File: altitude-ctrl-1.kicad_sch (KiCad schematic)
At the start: 92 parts, among them J1 Conn_01x02, J11 Conn_01x05, J2 TC2030, J3 Conn_01x02, J4 Conn_01x02, J5 Conn_01x04_Pin, J6 Conn_01x02, J7 Conn_01x02, J8 Conn_01x05, J9 Conn_01x05, SW1 SW_Push, SW2 SW_Push, SW3 SW_Push, SW4 SW_SPST, SW5 SW_SPST, U1 SN65HVD230, U2 LM73100, U3 HT753-1, U4 STM32F103C8Tx, U5 LM73100, U6 MAX6675, U8 ULN2003A, Y1 8M

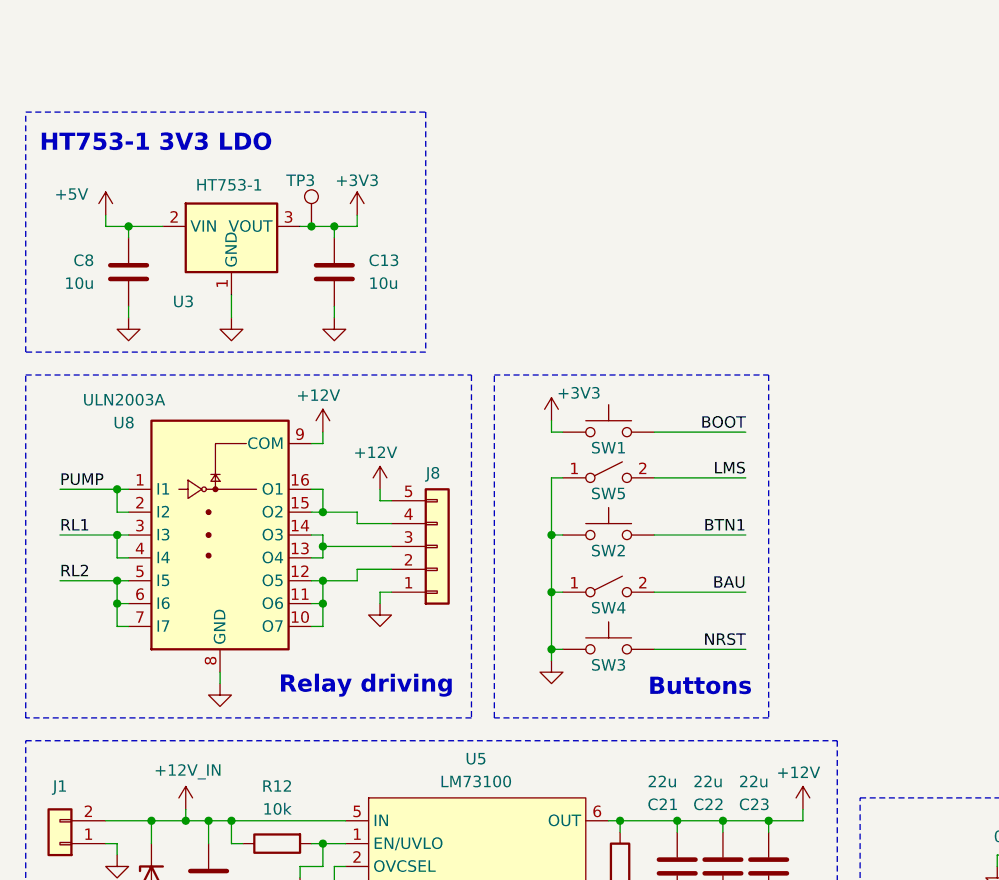
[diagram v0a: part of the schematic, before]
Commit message: schem: add test points
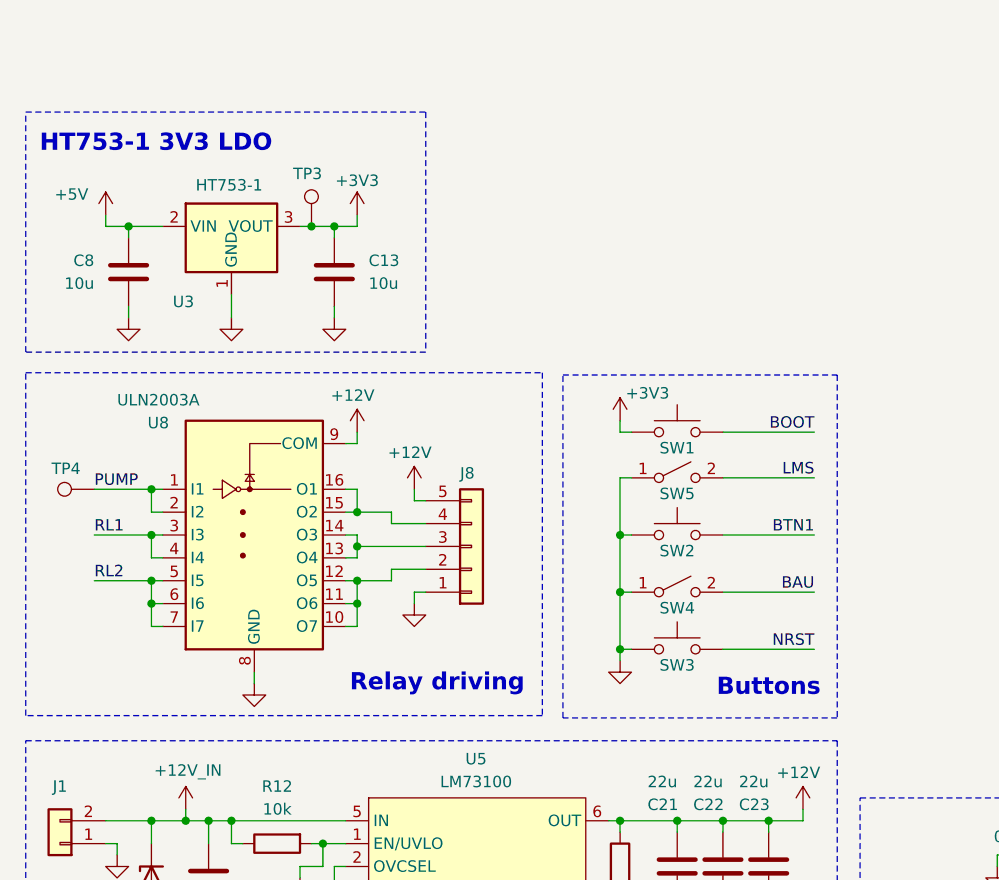
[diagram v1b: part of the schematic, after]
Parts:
- added TP4: TestPoint, TestPoint:TestPoint_Pad_D2.0mm, symbol Connector:TestPoint
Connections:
- net PUMP: now also TP4.1
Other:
- moved on the sheet: J8, SW1, SW2, SW3, SW4, SW5, U8

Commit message: schem: run and fix ERC
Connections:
- no-connect marks 14 -> 15

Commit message: schem: add missing footprints
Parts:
- J1, J6, J7, SW4, SW5, TC1: footprint (none) -> TerminalBlock_Phoenix:TerminalBlock_Phoenix_MKDS-1,5-2-5.08_1x02_P5.08mm_Horizontal
- J11, J8, J9: footprint (none) -> TerminalBlock_Phoenix:TerminalBlock_Phoenix_MKDS-1,5-5-5.08_1x05_P5.08mm_Horizontal
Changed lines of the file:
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@@
 			)
 		)
-		(property "Footprint" ""
+		(property "Footprint" "TerminalBlock_Phoenix:TerminalBlock_Phoenix_MKDS-1,5-2-5.08_1x02_P5.08mm_Horizontal"
 			(at 270.51 46.99 0)
 			(hide yes)
@@
 			)
 		)
-		(property "Footprint" ""
+		(property "Footprint" "TerminalBlock_Phoenix:TerminalBlock_Phoenix_MKDS-1,5-2-5.08_1x02_P5.08mm_Horizontal"
 			(at 17.78 165.1 0)
 			(hide yes)
@@
 			)
 		)
-		(property "Footprint" ""
+		(property "Footprint" "TerminalBlock_Phoenix:TerminalBlock_Phoenix_MKDS-1,5-2-5.08_1x02_P5.08mm_Horizontal"
 			(at 97.155 133.35 0)
 			(hide yes)
@@
 			)
 		)
-		(property "Footprint" ""
+		(property "Footprint" "TerminalBlock_Phoenix:TerminalBlock_Phoenix_MKDS-1,5-5-5.08_1x05_P5.08mm_Horizontal"
 			(at 63.5 87.63 0)
 			(hide yes)
@@
 			)
 		)
-		(property "Footprint" ""
+		(property "Footprint" "TerminalBlock_Phoenix:TerminalBlock_Phoenix_MKDS-1,5-5-5.08_1x05_P5.08mm_Horizontal"
 			(at 274.32 109.22 0)
 			(hide yes)
@@
 			)
 		)
-		(property "Footprint" ""
+		(property "Footprint" "TerminalBlock_Phoenix:TerminalBlock_Phoenix_MKDS-1,5-2-5.08_1x02_P5.08mm_Horizontal"
 			(at 86.36 80.01 0)
 			(hide yes)
@@
 			)
 		)
-		(property "Footprint" ""
+		(property "Footprint" "TerminalBlock_Phoenix:TerminalBlock_Phoenix_MKDS-1,5-2-5.08_1x02_P5.08mm_Horizontal"
 			(at 17.78 120.65 0)
 			(hide yes)
@@
 			)
 		)
-		(property "Footprint" ""
+		(property "Footprint" "TerminalBlock_Phoenix:TerminalBlock_Phoenix_MKDS-1,5-5-5.08_1x05_P5.08mm_Horizontal"
 			(at 274.32 77.47 0)
 			(hide yes)
@@
 			)
 		)
-		(property "Footprint" ""
+		(property "Footprint" "TerminalBlock_Phoenix:TerminalBlock_Phoenix_MKDS-1,5-2-5.08_1x02_P5.08mm_Horizontal"
 			(at 86.36 92.71 0)
 			(hide yes)

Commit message: schem: update exlude from BOM
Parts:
- J1, J11, J3, J4, J6, J7, J8, J9, SW4, SW5, TC1: now left out of the parts list
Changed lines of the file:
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@@
 		(body_style 1)
 		(exclude_from_sim no)
-		(in_bom yes)
+		(in_bom no)
 		(on_board yes)
 		(in_pos_files yes)
@@
 		(body_style 1)
 		(exclude_from_sim no)
-		(in_bom yes)
+		(in_bom no)
 		(on_board yes)
 		(in_pos_files yes)
@@
 		(body_style 1)
 		(exclude_from_sim no)
-		(in_bom yes)
+		(in_bom no)
 		(on_board yes)
 		(in_pos_files yes)
@@
 		(body_style 1)
 		(exclude_from_sim no)
-		(in_bom yes)
+		(in_bom no)
 		(on_board yes)
 		(in_pos_files yes)
@@
 		(body_style 1)
 		(exclude_from_sim no)
-		(in_bom yes)
+		(in_bom no)
 		(on_board yes)
 		(in_pos_files yes)
@@
 		(body_style 1)
 		(exclude_from_sim no)
-		(in_bom yes)
+		(in_bom no)
 		(on_board yes)
 		(in_pos_files yes)
@@
 		(body_style 1)
 		(exclude_from_sim no)
-		(in_bom yes)
+		(in_bom no)
 		(on_board yes)
 		(in_pos_files yes)
@@
 		(body_style 1)
 		(exclude_from_sim no)
-		(in_bom yes)
+		(in_bom no)
 		(on_board yes)
 		(in_pos_files yes)
@@
 		(body_style 1)
 		(exclude_from_sim no)
-		(in_bom yes)
+		(in_bom no)
 		(on_board yes)
 		(in_pos_files yes)
@@
 		(body_style 1)
 		(exclude_from_sim no)
-		(in_bom yes)
+		(in_bom no)
 		(on_board yes)
 		(in_pos_files yes)
@@
 		(body_style 1)
 		(exclude_from_sim no)
-		(in_bom yes)
+		(in_bom no)
 		(on_board yes)
 		(in_pos_files yes)

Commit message: schem: add title
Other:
- company: (none) -> 6NAPSE
- title: (none) -> Altitude CTRL 1
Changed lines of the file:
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@@
 	(generator_version "10.0")
 	(paper "A4")
+	(title_block
+		(title "Altitude CTRL 1")
+		(date "2026-07-08")
+		(rev "01")
+		(company "6NAPSE")
+	)
 	(rectangle
 		(start 106.68 115.57)

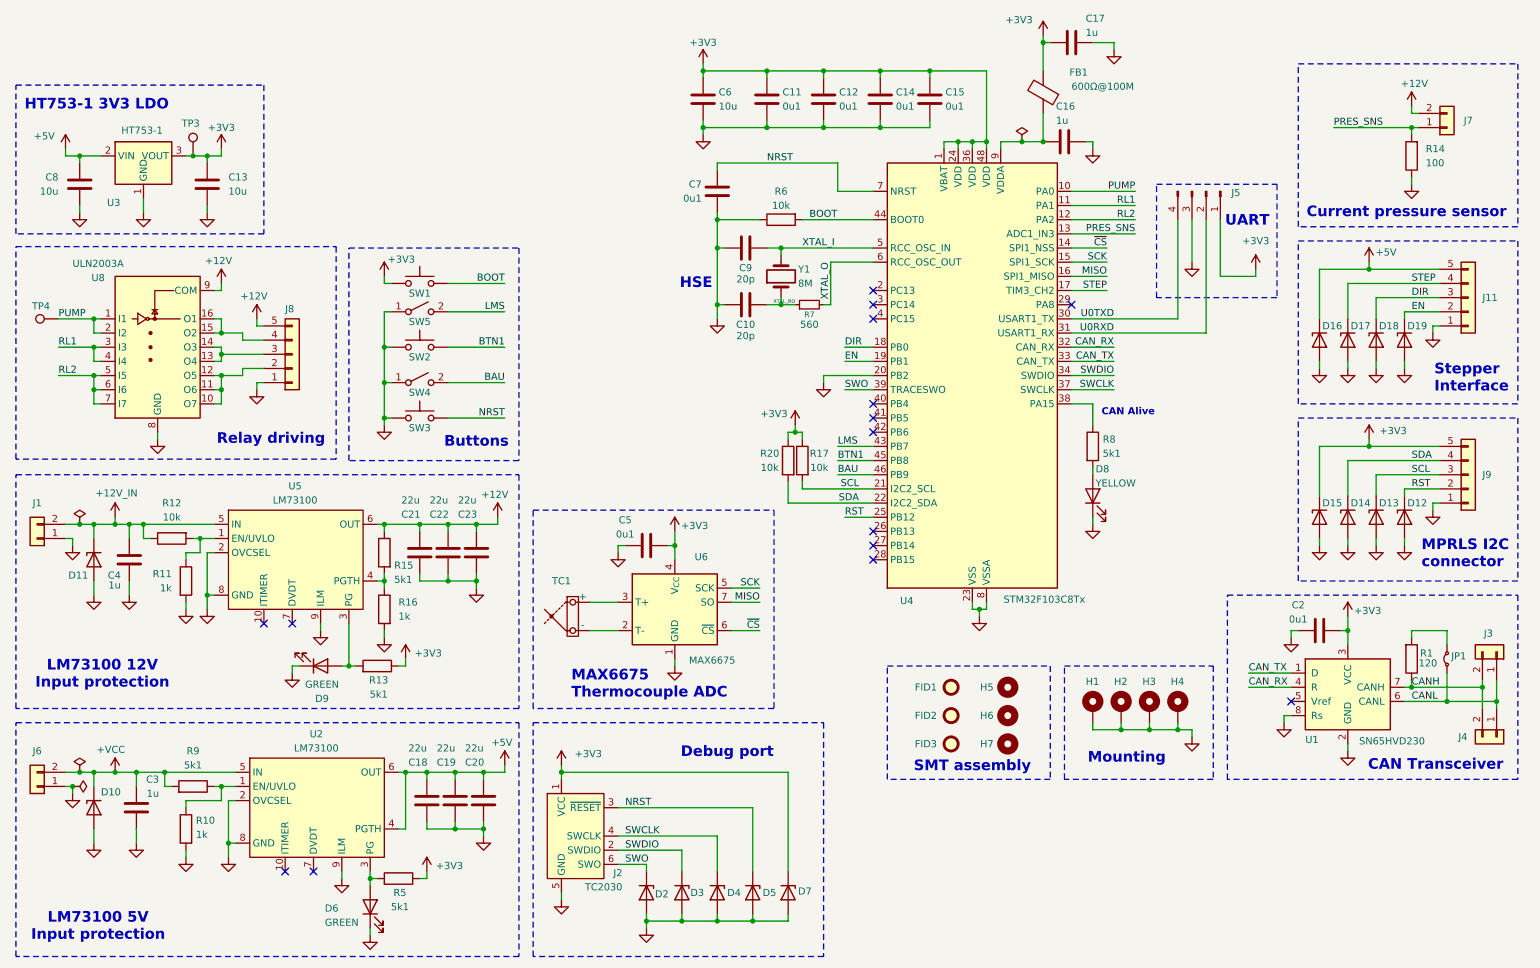
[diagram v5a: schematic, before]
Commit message: schem: renumber
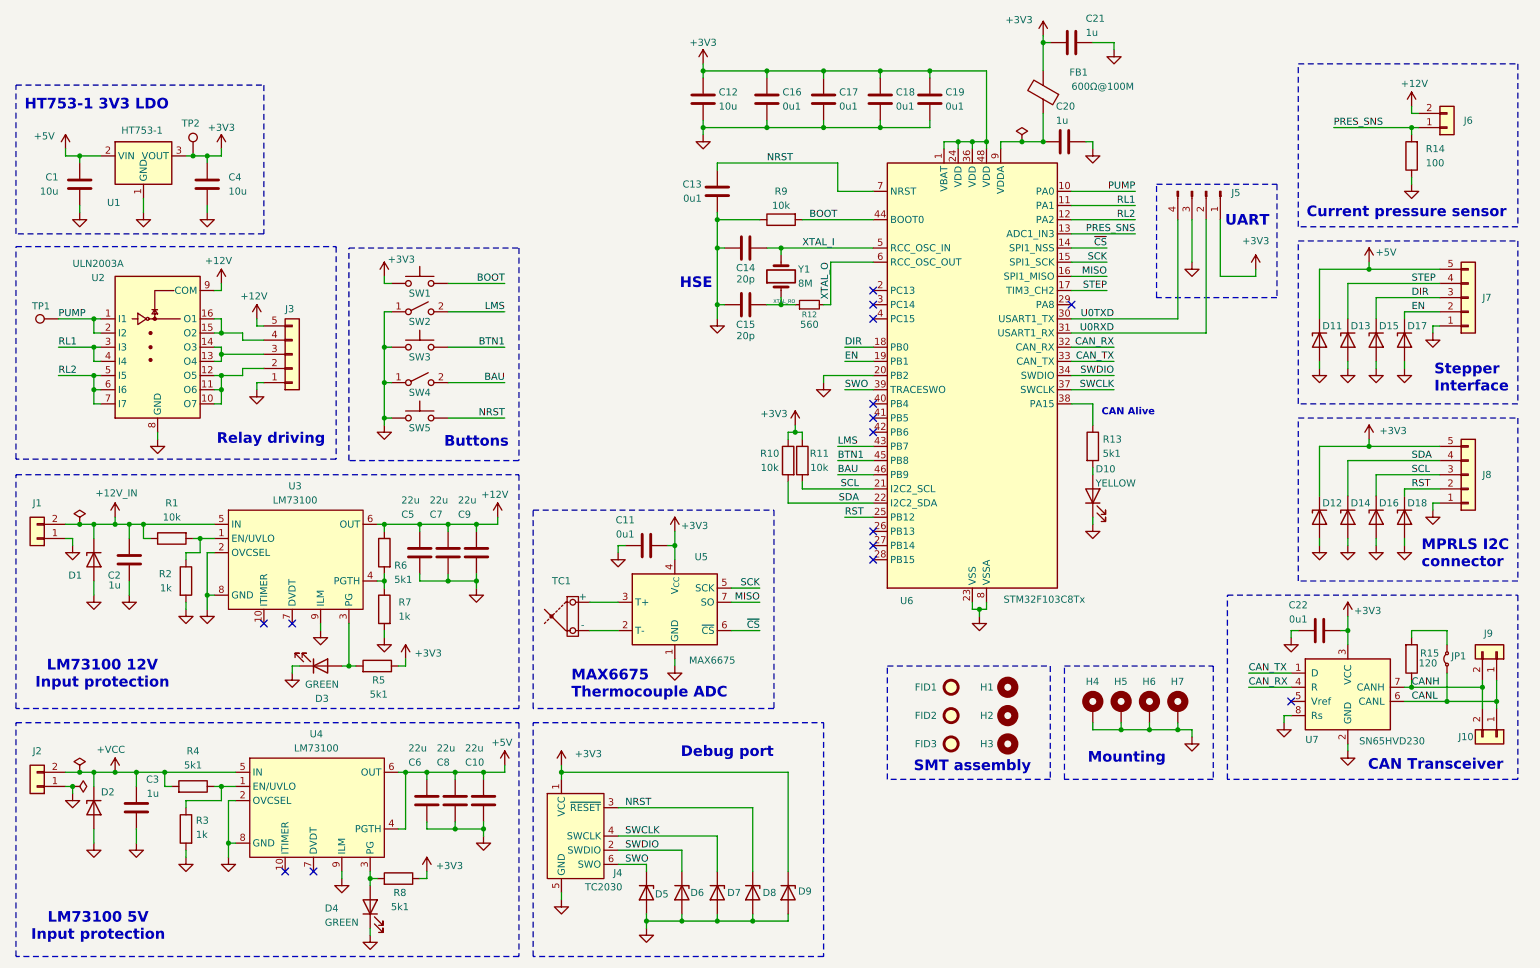
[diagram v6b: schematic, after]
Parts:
- renumbered C8 to C1, C20 to C10, C5 to C11, C6 to C12, C7 to C13, C9 to C14, C10 to C15, C11 to C16, C12 to C17, C14 to C18, C15 to C19, C4 to C2, C16 to C20, C17 to C21, C2 to C22, C13 to C4, C21 to C5, C18 to C6, C22 to C7, C19 to C8, C23 to C9, D11 to D1, D8 to D10, D16 to D11, D15 to D12, D17 to D13, D18 to D15, D13 to D16, D19 to D17, D12 to D18, D10 to D2, D9 to D3, D6 to D4, D2 to D5, D3 to D6, D4 to D7, D5 to D8, D7 to D9, H5 to H1, H6 to H2, H7 to H3, H1 to H4, H2 to H5, H3 to H6, H4 to H7, J4 to J10, J6 to J2, J8 to J3, J2 to J4, J7 to J6, J11 to J7, J9 to J8, J3 to J9, R12 to R1, R20 to R10, R17 to R11, R7 to R12, R8 to R13, R1 to R15, R11 to R2, R10 to R3, R9 to R4, R13 to R5, R15 to R6, R16 to R7, R5 to R8, R6 to R9, SW5 to SW2, SW2 to SW3, SW3 to SW5, TP4 to TP1, TP3 to TP2, U3 to U1, U8 to U2, U5 to U3, U2 to U4, U6 to U5, U4 to U6, U1 to U7

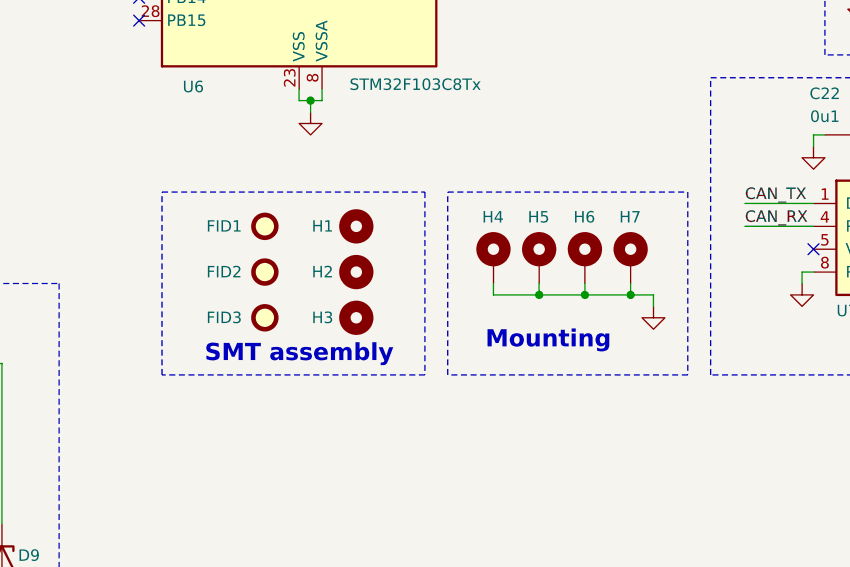
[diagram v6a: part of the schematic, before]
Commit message: pcb: edit board outline
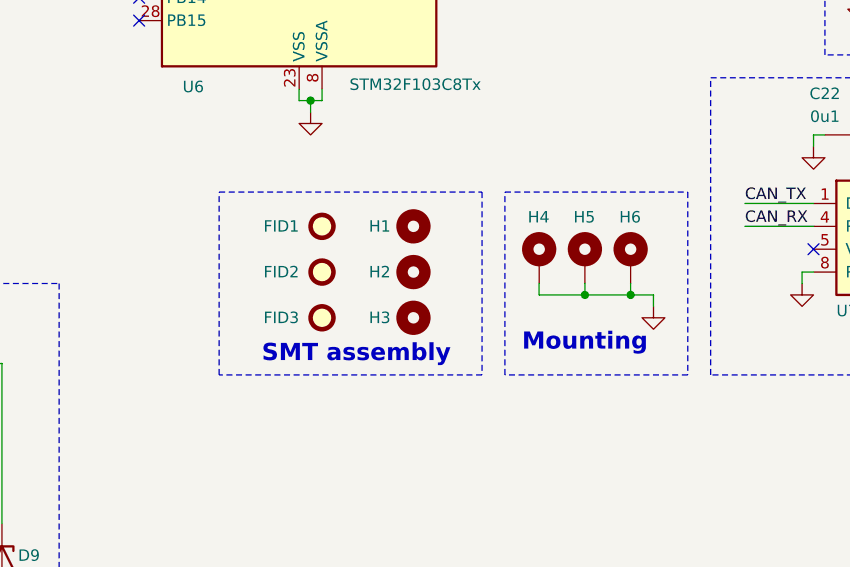
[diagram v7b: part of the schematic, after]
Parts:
- removed H7: MountingHole_Pad, MountingHole:MountingHole_3.2mm_M3_Pad_Via, symbol Mechanical:MountingHole_Pad
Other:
- moved on the sheet: FID1, FID2, FID3, H1, H2, H3, H4, H5, H6

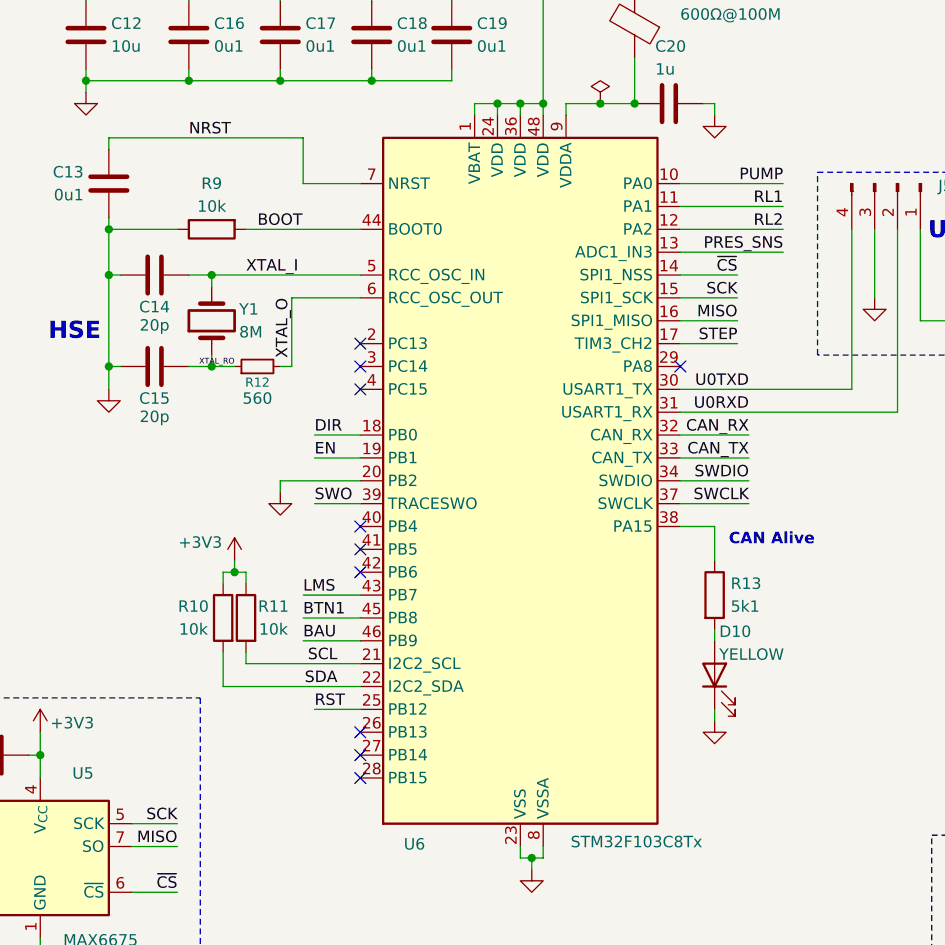
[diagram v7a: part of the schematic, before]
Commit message: pcb: reorganize programmable gpios
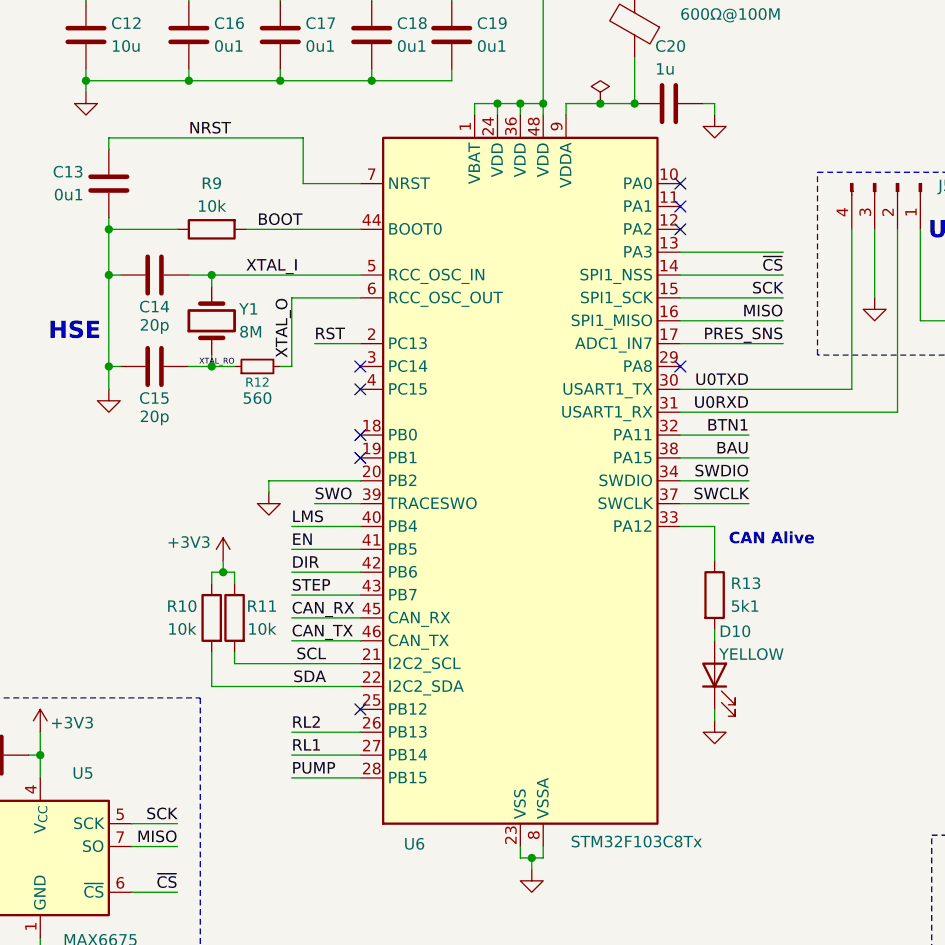
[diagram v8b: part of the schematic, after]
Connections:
- net BAU: now also U6.38 (PA15); no longer U6.46 (PB9)
- net BTN1: now also U6.32 (PA11); no longer U6.45 (PB8)
- net CAN_RX: now also U6.45 (PB8); no longer U6.32 (PA11)
- net CAN_TX: now also U6.46 (PB9); no longer U6.33 (PA12)
- net DIR: now also U6.42 (PB6); no longer U6.18 (PB0)
- net EN: now also U6.41 (PB5); no longer U6.19 (PB1)
- net LMS: now also U6.40 (PB4); no longer U6.43 (PB7)
- net PRES_SNS: now also U6.17 (PA7); no longer U6.13 (PA3)
- net PUMP: now also U6.28 (PB15); no longer U6.10 (PA0)
- net RL1: now also U6.27 (PB14); no longer U6.11 (PA1)
- net RL2: now also U6.26 (PB13); no longer U6.12 (PA2)
- net RST: now also U6.2 (PC13); no longer U6.25 (PB12)
- net STEP: now also U6.43 (PB7); no longer U6.17 (PA7)
- net at R13.1: now also U6.33 (PA12); no longer U6.38 (PA15)
- no-connect marks 15 -> 14
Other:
- moved on the sheet: R10, R11
